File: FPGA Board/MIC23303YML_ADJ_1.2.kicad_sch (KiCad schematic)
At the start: 24 parts, among them U5 MIC23303YML-TR

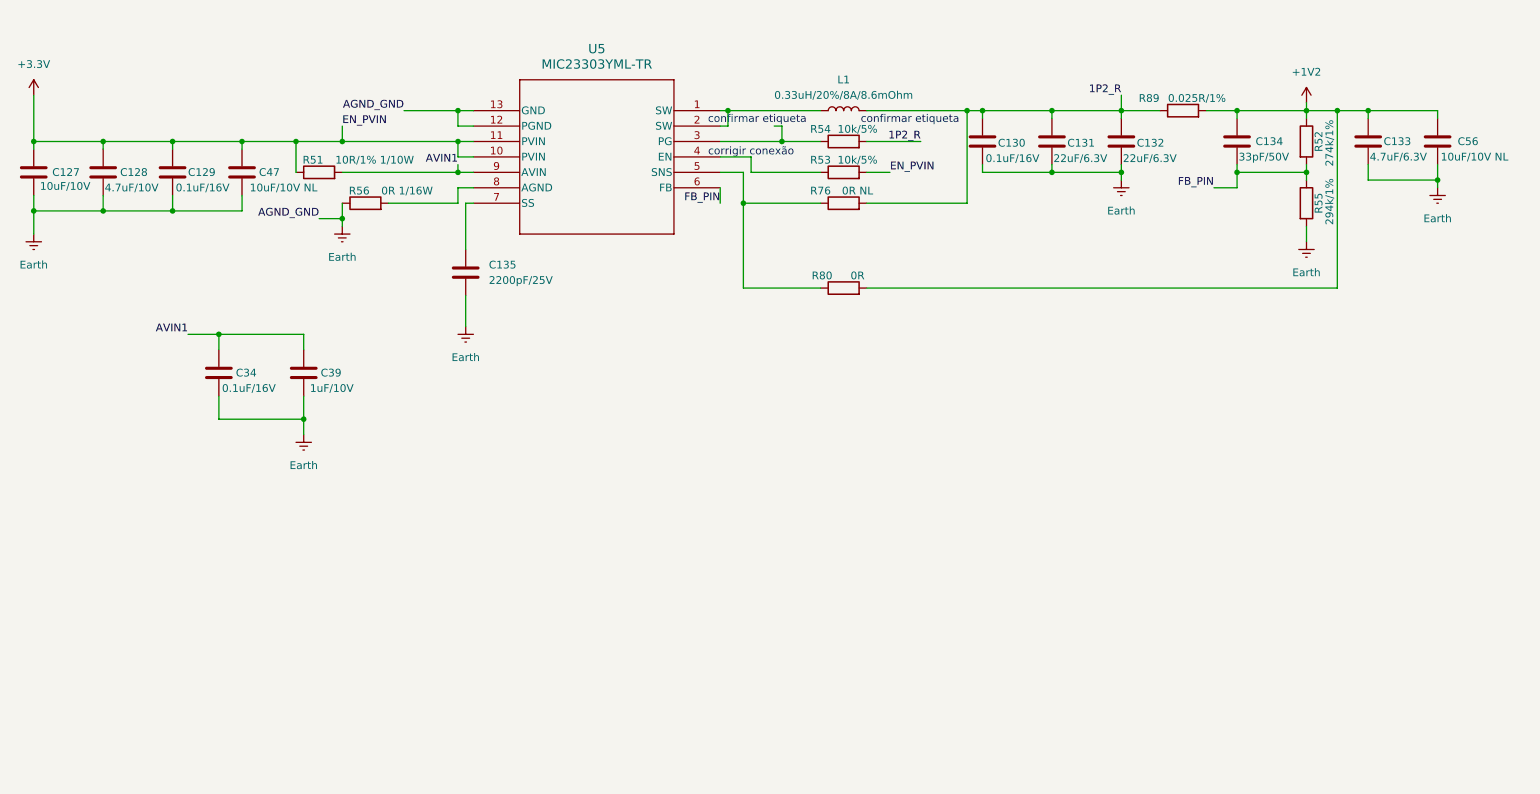
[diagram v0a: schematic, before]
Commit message: Inclusão do projeto KiCad, datasheets, símbolos, footprints, modelos 3D, correções de etiquetas hierarquicas e globais.
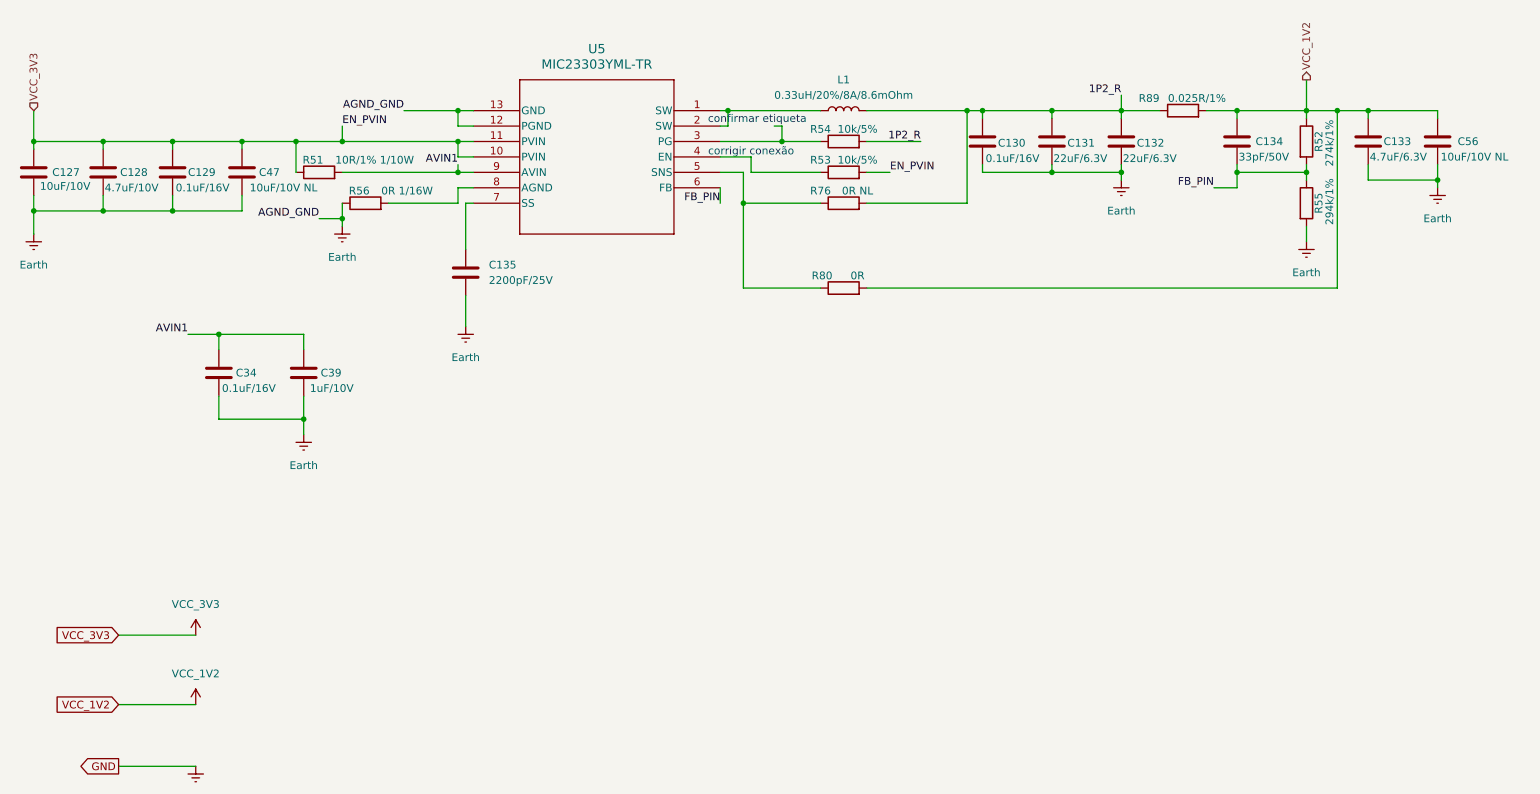
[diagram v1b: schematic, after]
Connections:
- net +1V2 renamed VCC_1V2
- net +3.3V renamed VCC_3V3
